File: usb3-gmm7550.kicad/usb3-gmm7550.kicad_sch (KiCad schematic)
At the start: 3 parts

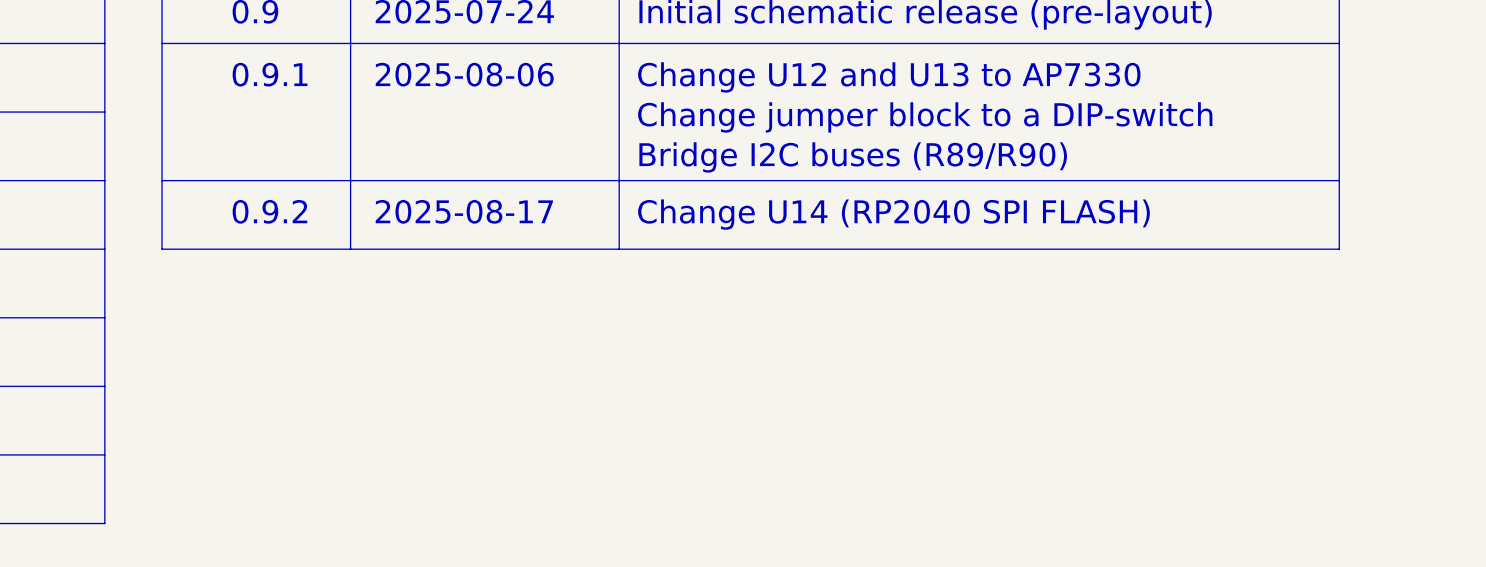
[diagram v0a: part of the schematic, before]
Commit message: Add USB Type-C plug polarity indication (A_B_SIDE signal from PD controller)
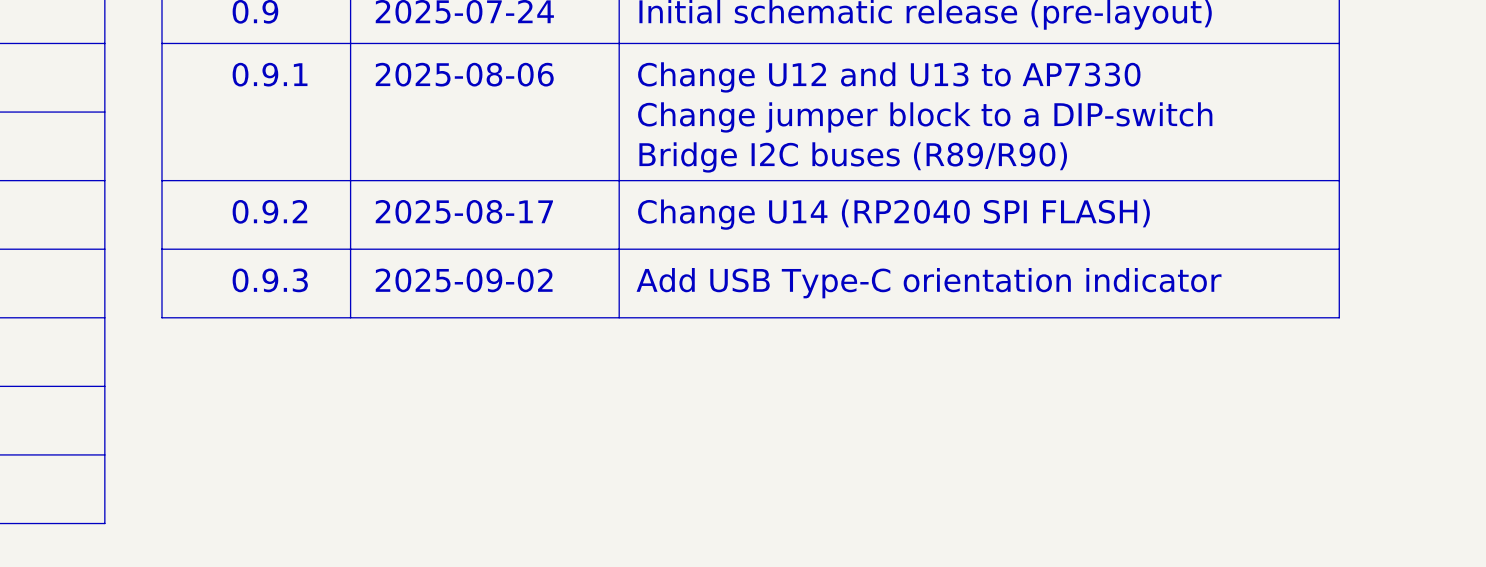
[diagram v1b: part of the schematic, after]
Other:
- note added: "0.9.3"
- note added: "2025-09-02"
- note added: "Add USB Type-C orientation indicator"
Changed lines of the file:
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@@
 	(title_block
 		(title "GMM-7550 USB3 Adapter")
-		(date "2025-08-17")
-		(rev "0.9.2")
+		(date "2025-09-02")
+		(rev "0.9.3")
 	)
 	(text "Sheet #"
@@
 		(exclude_from_sim no)
 		(at 29.21 99.695 0)
+		(effects
+			(font
+				(size 2.54 2.54)
+				(thickness 0.3175)
+			)
+			(justify left)
+		)
+	)
+	(text "2025-09-02"
+		(exclude_from_sim no)
+		(at 172.085 83.82 0)
 		(effects
 			(font
@@
 		)
 	)
+	(text "0.9.3"
+		(exclude_from_sim no)
+		(at 156.21 83.82 0)
+		(effects
+			(font
+				(size 2.54 2.54)
+				(thickness 0.3175)
+			)
+			(justify left)
+		)
+	)
 	(text "2025-07-24"
 		(exclude_from_sim no)
@@
 			(font
 				(size 1.27 1.27)
+			)
+			(justify left)
+		)
+	)
+	(text "Add USB Type-C orientation indicator"
+		(exclude_from_sim no)
+		(at 201.295 83.82 0)
+		(effects
+			(font
+				(size 2.54 2.54)
+				(thickness 0.3175)
 			)
 			(justify left)
@@
 	(polyline
 		(pts
+			(xy 169.545 80.01) (xy 169.545 87.63)
+		)
+		(stroke
+			(width 0)
+			(type default)
+		)
+	)
+	(polyline
+		(pts
 			(xy 279.4 41.91) (xy 279.4 57.15)
 		)
@@
 	(polyline
 		(pts
+			(xy 199.39 80.01) (xy 199.39 87.63)
+		)
+		(stroke
+			(width 0)
+			(type default)
+		)
+	)
+	(polyline
+		(pts
 			(xy 21.59 80.01) (xy 142.24 80.01)
 		)
@@
 	(polyline
 		(pts
+			(xy 279.4 80.01) (xy 279.4 87.63)
+		)
+		(stroke
+			(width 0)
+			(type default)
+		)
+	)
+	(polyline
+		(pts
 			(xy 199.39 72.39) (xy 199.39 80.01)
 		)
@@
 		)
 		(stroke
+			(width 0)
+			(type default)
+		)
+	)
+	(polyline
+		(pts
+			(xy 148.59 80.01) (xy 148.59 87.63)
+		)
+		(stroke
+			(width 0)
+			(type default)
+		)
+	)
+	(polyline
+		(pts
+			(xy 279.4 87.63) (xy 148.59 87.63)
+		)
+		(stroke

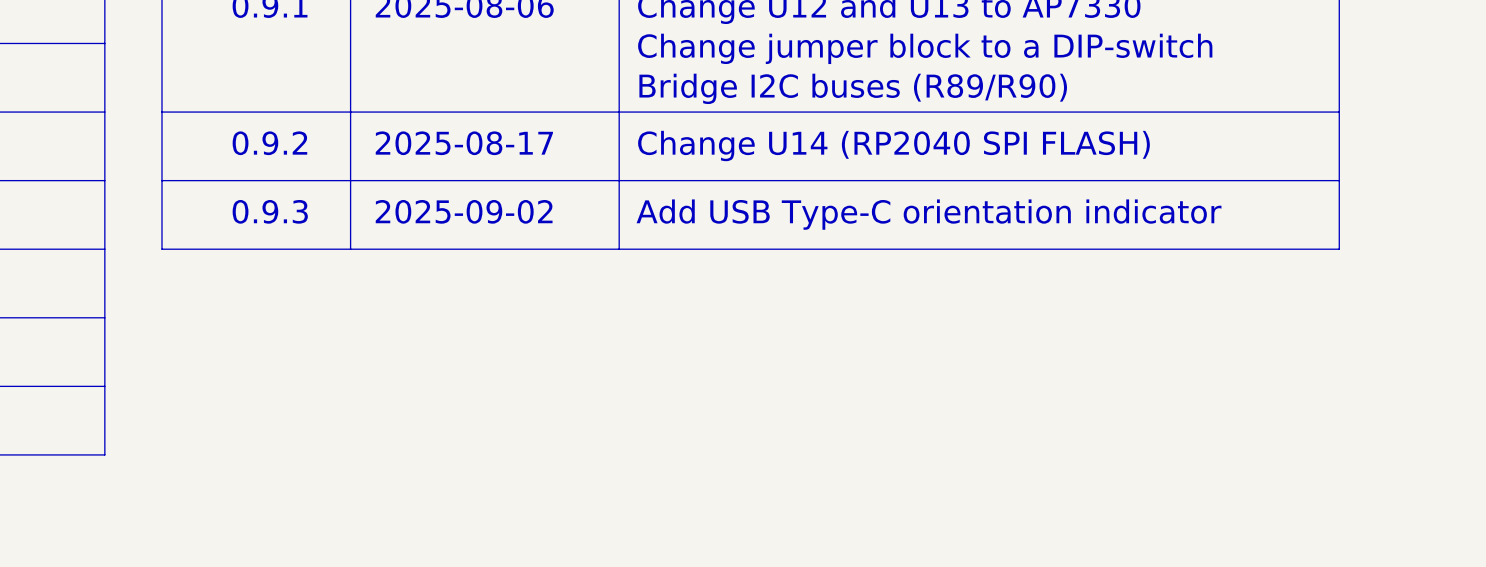
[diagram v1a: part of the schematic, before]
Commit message: Layout -- re-arrange and connect all GMM-7550 IOs on J4 (USB 1.1 and 2.0)
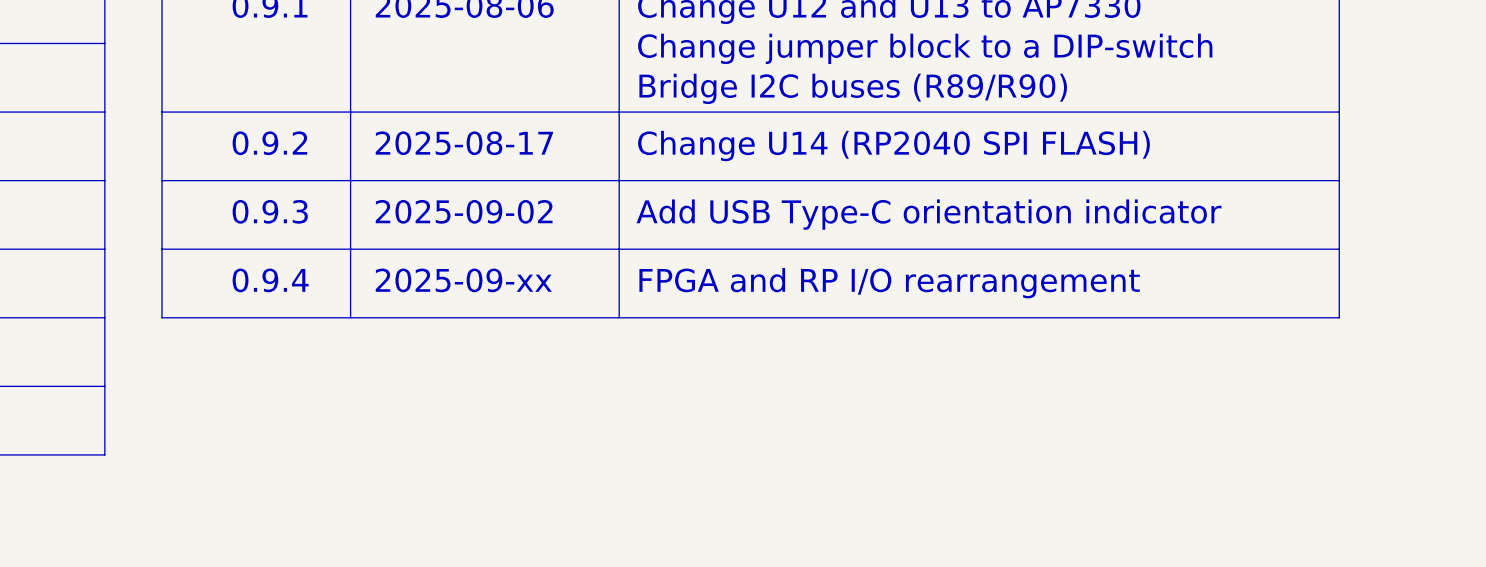
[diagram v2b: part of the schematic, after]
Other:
- note added: "0.9.4"
- note added: "2025-09-xx"
- note added: "FPGA and RP I/O rearrangement"
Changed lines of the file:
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@@
 	(title_block
 		(title "GMM-7550 USB3 Adapter")
-		(date "2025-09-02")
-		(rev "0.9.3")
+		(date "2025-09-xx")
+		(rev "0.9.4")
 	)
 	(text "Sheet #"
@@
 		(exclude_from_sim no)
 		(at 45.72 76.835 0)
+		(effects
+			(font
+				(size 2.54 2.54)
+				(thickness 0.3175)
+			)
+			(justify left)
+		)
+	)
+	(text "FPGA and RP I/O rearrangement"
+		(exclude_from_sim no)
+		(at 201.295 91.44 0)
+		(effects
+			(font
+				(size 2.54 2.54)
+				(thickness 0.3175)
+			)
+			(justify left)
+		)
+	)
+	(text "2025-09-xx"
+		(exclude_from_sim no)
+		(at 172.085 91.44 0)
 		(effects
 			(font
@@
 		)
 	)
+	(text "0.9.4"
+		(exclude_from_sim no)
+		(at 156.21 91.44 0)
+		(effects
+			(font
+				(size 2.54 2.54)
+				(thickness 0.3175)
+			)
+			(justify left)
+		)
+	)
 	(text "GMM-7550 Module Power and Control"
 		(exclude_from_sim no)
@@
 	(polyline
 		(pts
+			(xy 279.4 95.25) (xy 148.59 95.25)
+		)
+		(stroke
+			(width 0)
+			(type default)
+		)
+	)
+	(polyline
+		(pts
 			(xy 21.59 110.49) (xy 22.225 110.49)
 		)
@@
 	(polyline
 		(pts
+			(xy 148.59 87.63) (xy 148.59 95.25)
+		)
+		(stroke
+			(width 0)
+			(type default)
+		)
+	)
+	(polyline
+		(pts
 			(xy 169.545 72.39) (xy 169.545 80.01)
 		)
@@
 	(polyline
 		(pts
+			(xy 279.4 87.63) (xy 279.4 95.25)
+		)
+		(stroke
+			(width 0)
+			(type default)
+		)
+	)
+	(polyline
+		(pts
 			(xy 41.91 41.91) (xy 41.91 110.49)
 		)
@@
 	(polyline
 		(pts
+			(xy 169.545 87.63) (xy 169.545 95.25)
+		)
+		(stroke
+			(width 0)
+			(type default)
+		)
+	)
+	(polyline
+		(pts
 			(xy 21.59 64.77) (xy 142.24 64.77)
 		)
@@
 		)
 		(stroke
+			(width 0)
+			(type default)
+		)
+	)
+	(polyline
+		(pts
+			(xy 199.39 87.63) (xy 199.39 95.25)
+		)
+		(stroke

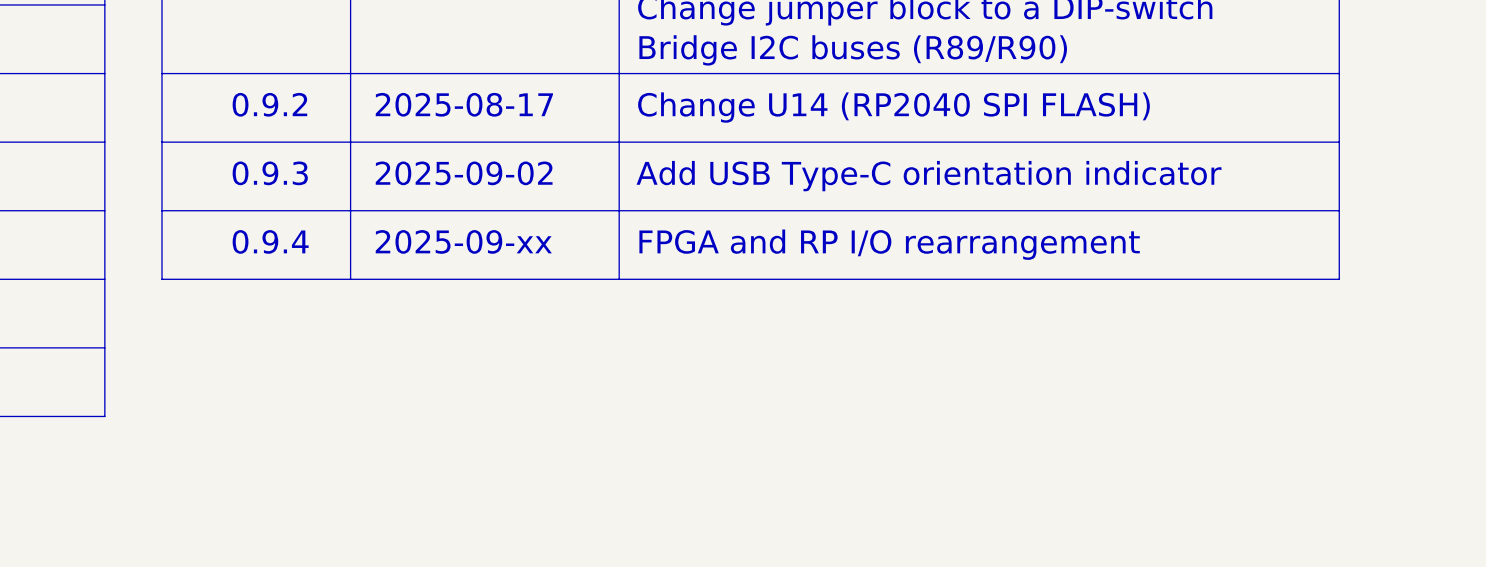
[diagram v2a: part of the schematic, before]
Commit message: USB Power Delivery redesign (STmicro controller is NRND)
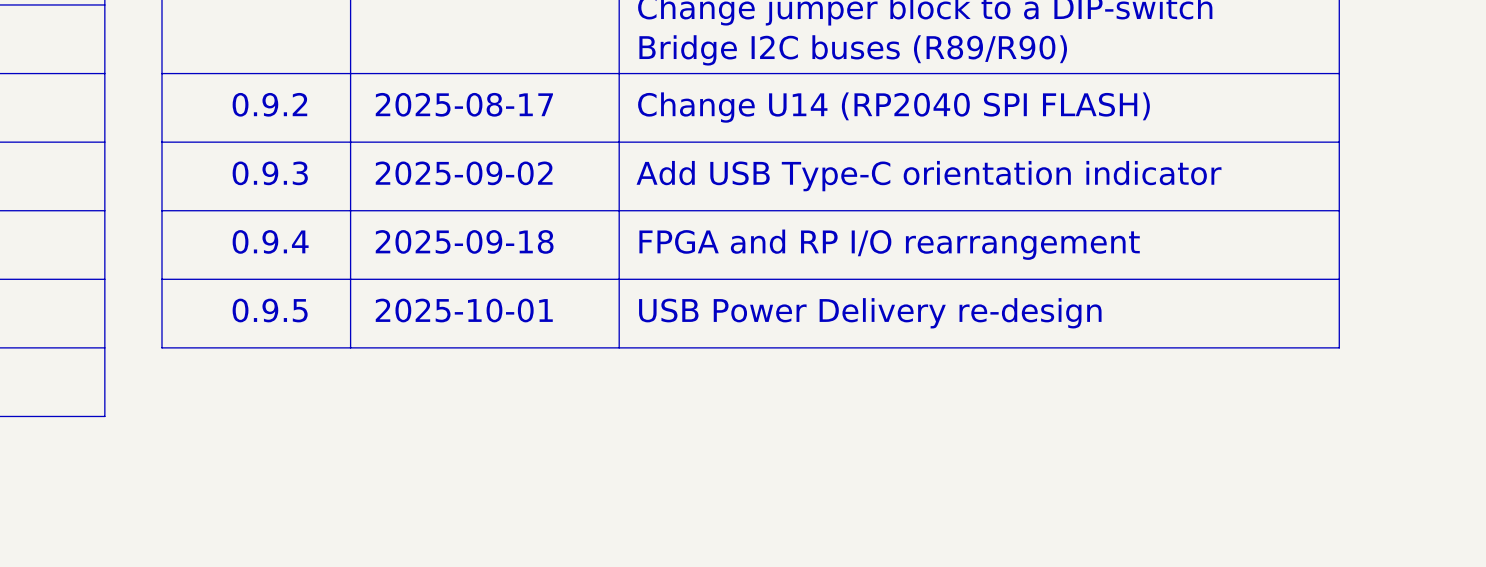
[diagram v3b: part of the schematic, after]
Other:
- note added: "0.9.5"
- note added: "2025-09-18"
- note added: "2025-10-01"
- note added: "USB Power Delivery re-design"
- note removed: "2025-09-xx"
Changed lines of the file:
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@@
 	(title_block
 		(title "GMM-7550 USB3 Adapter")
-		(date "2025-09-xx")
-		(rev "0.9.4")
+		(date "2025-10-01")
+		(rev "0.9.5")
 	)
 	(text "Sheet #"
@@
 		)
 	)
+	(text "USB Power Delivery re-design"
+		(exclude_from_sim no)
+		(at 201.295 99.06 0)
+		(effects
+			(font
+				(size 2.54 2.54)
+				(thickness 0.3175)
+			)
+			(justify left)
+		)
+	)
 	(text "Revision"
 		(exclude_from_sim no)
@@
 		)
 	)
-	(text "2025-09-xx"
+	(text "2025-09-18"
 		(exclude_from_sim no)
 		(at 172.085 91.44 0)
@@
 		(exclude_from_sim no)
 		(at 29.21 92.075 0)
+		(effects
+			(font
+				(size 2.54 2.54)
+				(thickness 0.3175)
+			)
+			(justify left)
+		)
+	)
+	(text "0.9.5"
+		(exclude_from_sim no)
+		(at 156.21 99.06 0)
 		(effects
 			(font
@@
 		)
 	)
+	(text "2025-10-01"
+		(exclude_from_sim no)
+		(at 172.085 99.06 0)
+		(effects
+			(font
+				(size 2.54 2.54)
+				(thickness 0.3175)
+			)
+			(justify left)
+		)
+	)
 	(text "2025-08-06"
 		(exclude_from_sim no)
@@
 	(polyline
 		(pts
+			(xy 279.4 95.25) (xy 279.4 102.87)
+		)
+		(stroke
+			(width 0)
+			(type default)
+		)
+	)
+	(polyline
+		(pts
 			(xy 169.545 72.39) (xy 169.545 80.01)
 		)
@@
 	(polyline
 		(pts
+			(xy 169.545 95.25) (xy 169.545 102.87)
+		)
+		(stroke
+			(width 0)
+			(type default)
+		)
+	)
+	(polyline
+		(pts
 			(xy 21.59 110.49) (xy 142.24 110.49)
 		)
@@
 	(polyline
 		(pts
+			(xy 199.39 95.25) (xy 199.39 102.87)
+		)
+		(stroke
+			(width 0)
+			(type default)
+		)
+	)
+	(polyline
+		(pts
 			(xy 279.4 41.91) (xy 279.4 57.15)
 		)
@@
 	(polyline
 		(pts
+			(xy 279.4 102.87) (xy 148.59 102.87)
+		)
+		(stroke
+			(width 0)
+			(type default)
+		)
+	)
+	(polyline
+		(pts
 			(xy 279.4 87.63) (xy 279.4 95.25)
 		)
@@
 		)
 		(stroke
+			(width 0)
+			(type default)
+		)
+	)
+	(polyline
+		(pts
+			(xy 148.59 95.25) (xy 148.59 102.87)
+		)
+		(stroke

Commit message: Final touches -- revision 1.0 schematic is released
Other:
- note added: "1.0"
- note added: "Release to manufacturing"
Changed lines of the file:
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@@
 	(title_block
 		(title "GMM-7550 USB3 Adapter")
-		(date "2025-10-01")
-		(rev "0.9.5")
+		(date "2025-10-10")
+		(rev "1.0")
 	)
 	(text "Sheet #"
@@
 	(text "2025-09-02"
 		(exclude_from_sim no)
-		(at 172.085 83.82 0)
+		(at 172.085 84.455 0)
 		(effects
 			(font
@@
 	(text "USB Power Delivery re-design"
 		(exclude_from_sim no)
-		(at 201.295 99.06 0)
+		(at 201.295 99.695 0)
 		(effects
 			(font
@@
 		)
 	)
+	(text "Release to manufacturing"
+		(exclude_from_sim no)
+		(at 201.295 107.315 0)
+		(effects
+			(font
+				(size 2.54 2.54)
+				(thickness 0.3175)
+			)
+			(justify left)
+		)
+	)
 	(text "3"
 		(exclude_from_sim no)
@@
 	(text "2025-08-17"
 		(exclude_from_sim no)
-		(at 172.085 76.2 0)
+		(at 172.085 76.835 0)
 		(effects
 			(font
@@
 	(text "FPGA and RP I/O rearrangement"
 		(exclude_from_sim no)
-		(at 201.295 91.44 0)
+		(at 201.295 92.075 0)
 		(effects
 			(font
@@
 	(text "2025-09-18"
 		(exclude_from_sim no)
-		(at 172.085 91.44 0)
+		(at 172.085 92.075 0)
 		(effects
 			(font
@@
 	(text "Change U14 (RP2040 SPI FLASH)"
 		(exclude_from_sim no)
-		(at 201.295 76.2 0)
+		(at 201.295 76.835 0)
 		(effects
 			(font
@@
 	(text "0.9.5"
 		(exclude_from_sim no)
-		(at 156.21 99.06 0)
+		(at 156.21 99.695 0)
 		(effects
 			(font
@@
 		)
 	)
+	(text "1.0"
+		(exclude_from_sim no)
+		(at 156.21 107.315 0)
+		(effects
+			(font
+				(size 2.54 2.54)
+				(thickness 0.3175)
+			)
+			(justify left)
+		)
+	)
 	(text "Experimental USB 3 adapter for GMM-7550 Module"
 		(exclude_from_sim no)
@@
 	(text "0.9.2"
 		(exclude_from_sim no)
-		(at 156.21 76.2 0)
+		(at 156.21 76.835 0)
 		(effects
 			(font
@@
 	(text "0.9.3"
 		(exclude_from_sim no)
-		(at 156.21 83.82 0)
+		(at 156.21 84.455 0)
 		(effects
 			(font
@@
 	(text "2025-10-01"
 		(exclude_from_sim no)
-		(at 172.085 99.06 0)
+		(at 172.085 107.315 0)
+		(effects
+			(font
+				(size 2.54 2.54)
+				(thickness 0.3175)
+			)
+			(justify left)
+		)
+	)
+	(text "2025-10-01"
+		(exclude_from_sim no)
+		(at 172.085 99.695 0)
 		(effects
 			(font
@@
 	(text "Add USB Type-C orientation indicator"
 		(exclude_from_sim no)
-		(at 201.295 83.82 0)
+		(at 201.295 84.455 0)
 		(effects
 			(font
@@
 	(text "0.9.4"
 		(exclude_from_sim no)
-		(at 156.21 91.44 0)
+		(at 156.21 92.075 0)
 		(effects
 			(font
@@
 	(polyline
 		(pts
+			(xy 279.4 110.49) (xy 279.4 102.87)
+		)
+		(stroke
+			(width 0)
+			(type default)
+		)
+	)
+	(polyline
+		(pts
 			(xy 279.4 57.15) (xy 279.4 72.39)
 		)
@@
 	(polyline
 		(pts
+			(xy 199.39 102.87) (xy 199.39 110.49)
+		)
+		(stroke
+			(width 0)
+			(type default)
+		)
+	)
+	(polyline
+		(pts
+			(xy 148.59 110.49) (xy 279.4 110.49)
+		)
+		(stroke
+			(width 0)
+			(type default)
+		)
+	)
+	(polyline
+		(pts
 			(xy 279.4 80.01) (xy 148.59 80.01)
 		)
@@
 	(polyline
 		(pts
+			(xy 148.59 102.87) (xy 148.59 110.49)
+		)
+		(stroke
+			(width 0)
+			(type default)
+		)
+	)
+	(polyline
+		(pts
 			(xy 279.4 102.87) (xy 148.59 102.87)
 		)
@@
 	(polyline
 		(pts
+			(xy 169.545 102.87) (xy 169.545 110.49)
+		)
+		(stroke
+			(width 0)
+			(type default)
+		)
+	)
+	(polyline
+		(pts
 			(xy 169.545 87.63) (xy 169.545 95.25)
 		)
@@
 	)
 	(sheet
-		(at 24.13 181.61)
+		(at 107.95 181.61)
 		(size 12.7 8.89)
 		(exclude_from_sim no)
@@
 		)
 		(property "Sheetname" "USB PD"
-			(at 24.13 180.8984 0)
+			(at 107.95 180.8984 0)
 			(effects
 				(font
@@
 		)
 		(property "Sheetfile" "usb3-pd.kicad_sch"
-			(at 24.13 191.0846 0)
+			(at 107.95 191.0846 0)
 			(effects
 				(font

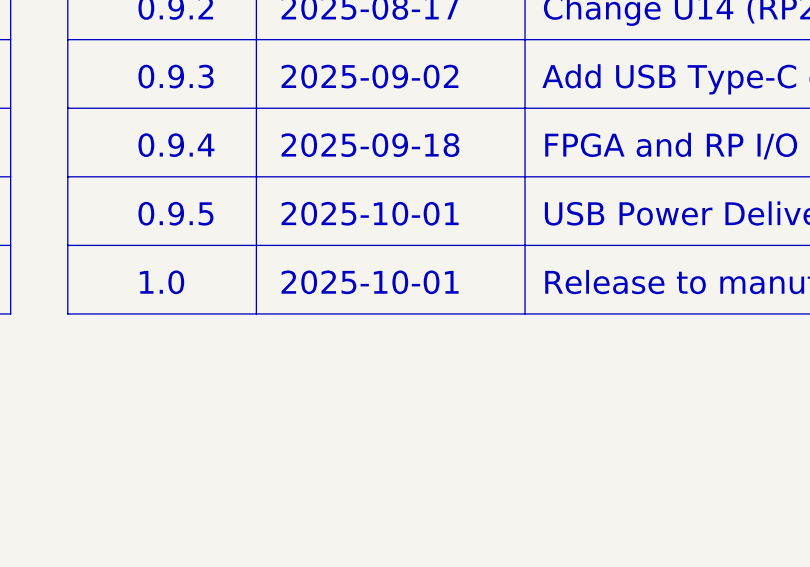
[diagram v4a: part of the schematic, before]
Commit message: Fix release date on the schematic title sheet and add a link to the schematic from README
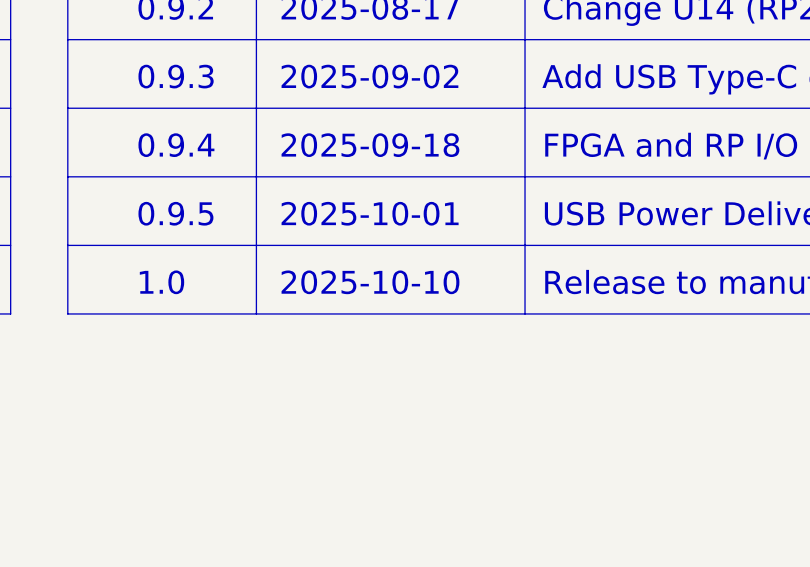
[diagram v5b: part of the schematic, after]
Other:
- note added: "2025-10-10"
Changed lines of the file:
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@@
 		)
 	)
-	(text "2025-10-01"
+	(text "2025-10-10"
 		(exclude_from_sim no)
 		(at 172.085 107.315 0)
